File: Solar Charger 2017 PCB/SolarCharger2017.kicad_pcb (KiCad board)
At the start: 2 copper layers, 95 x 65 mm, 24 parts, among them P1 5V OUT, P2 LiIon Cell V, P3 PV IN 1, P4 PV IN 2, P5 LiIon Cell V, P6 5V OUT, P7 USB_A, SW1 5V ON, U1 BQ24210

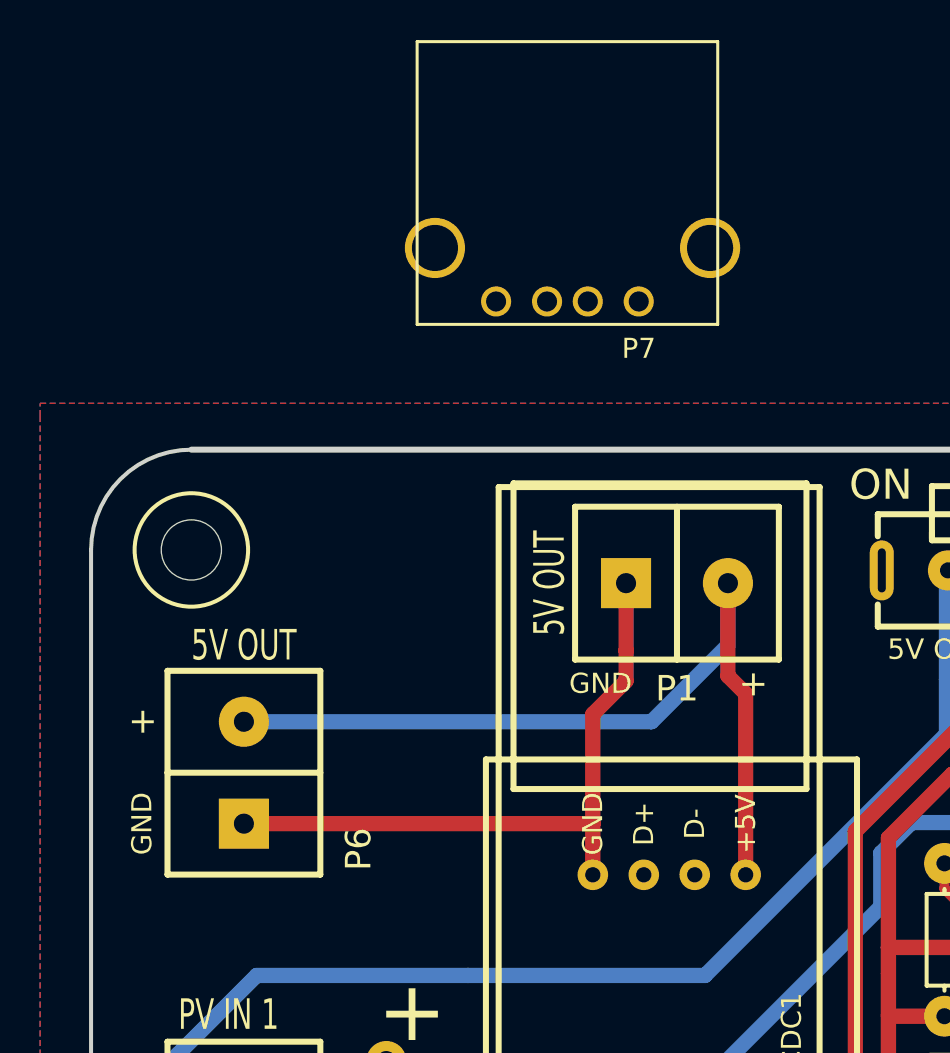
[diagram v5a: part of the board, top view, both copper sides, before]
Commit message: Update of PCB with USB output
Slight change to the USB output.
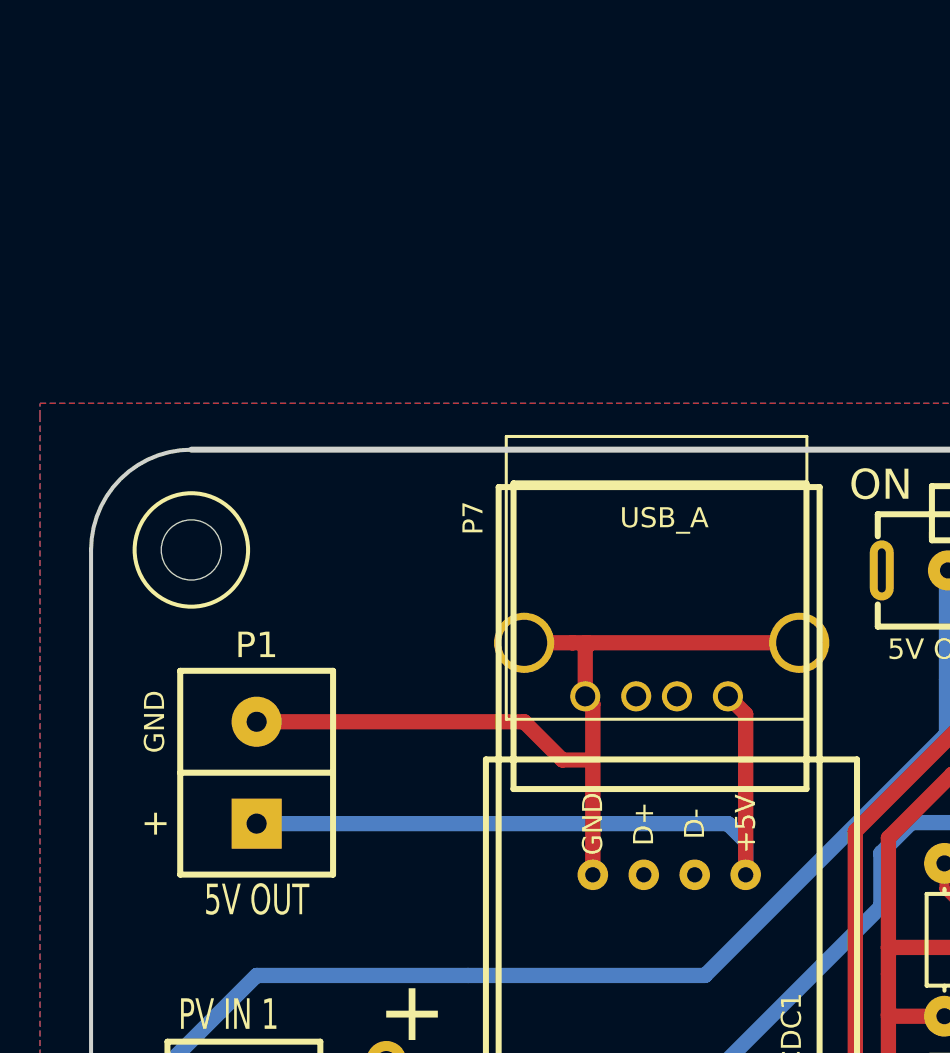
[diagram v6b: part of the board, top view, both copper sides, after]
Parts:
- removed P6: 5V OUT, REInnovationFootprint:SIL-2_screw_terminal
- moved P1 22.0 mm to (106.7, 82.5), turned to 90 degrees
- moved P7 20.2 mm to (130.2, 76.2)
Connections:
- P1 pad 1: Net-(DCDC1-Pad4) -> Net-(DCDC1-Pad3)
- P1 pad 2: Net-(DCDC1-Pad3) -> Net-(DCDC1-Pad4)
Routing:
- net Net-(DCDC1-Pad4): track 33.1 -> 43.3 mm
- net Net-(DCDC1-Pad3): track 43.7 -> 35.7 mm
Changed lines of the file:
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@@
 (kicad_pcb (version 4) (host pcbnew 4.0.5)
   (general
-    (links 51)
-    (no_connects 4)
+    (links 49)
+    (no_connects 0)
     (area 0 0 0 0)
     (thickness 1.6)
     (drawings 11)
-    (tracks 205)
+    (tracks 209)
     (zones 0)
-    (modules 24)
+    (modules 23)
     (nets 18)
   )
@@
   )
   (module REInnovationFootprint:SIL-2_screw_terminal (layer F.Cu)
-    (at 125.095 70.56)
+    (at 106.68 82.55 90)
     (descr "Connecteurs 2 pins")
     (tags "CONN DEV")
-    (fp_text reference P1 (at 2.54 5.259) (layer F.SilkS)
+    (fp_text reference P1 (at 8.89 0 180) (layer F.SilkS)
       (effects (font (thickness 0.3048)))
     )
-    (fp_text value "5V OUT" (at -3.81 0 270) (layer F.SilkS)
+    (fp_text value "5V OUT" (at -3.81 0 360) (layer F.SilkS)
       (effects (font (size 1.524 1.016) (thickness 0.254)))
     )
@@
     (fp_line (start 2.54 -3.81) (end 2.54 3.81) (layer F.SilkS) (width 0.3))
     (fp_line (start -2.54 3.81) (end -2.54 -3.81) (layer F.SilkS) (width 0.3))
-    (fp_text user GND (at -1.27 5.005) (layer F.SilkS)
+    (fp_text user GND (at 5.08 -5.08 90) (layer F.SilkS)
       (effects (font (size 1 1) (thickness 0.25)))
     )
-    (fp_text user + (at 6.35 5.005) (layer F.SilkS)
+    (fp_text user + (at 0 -5.08 90) (layer F.SilkS)
       (effects (font (thickness 0.3048)))
     )
-    (pad 1 thru_hole rect (at 0 0) (size 2.49936 2.49936) (drill 1.00076) (layers *.Cu *.Mask F.SilkS)
-      (net 12 "Net-(DCDC1-Pad4)"))
-    (pad 2 thru_hole circle (at 5.08 0) (size 2.49936 2.49936) (drill 1.00076) (layers *.Cu *.Mask F.SilkS)
+    (pad 1 thru_hole rect (at 0 0 90) (size 2.49936 2.49936) (drill 1.00076) (layers *.Cu *.Mask F.SilkS)
       (net 11 "Net-(DCDC1-Pad3)"))
+    (pad 2 thru_hole circle (at 5.08 0 90) (size 2.49936 2.49936) (drill 1.00076) (layers *.Cu *.Mask F.SilkS)
+      (net 12 "Net-(DCDC1-Pad4)"))
   )
   (module REInnovationFootprint:TH_LiIon_Holder (layer F.Cu)
@@
       (net 2 GND))
   )
-  (module REInnovationFootprint:SIL-2_screw_terminal (layer F.Cu)
-    (at 106.045 82.55 90)
-    (descr "Connecteurs 2 pins")
-    (tags "CONN DEV")
-    (fp_text reference P6 (at -1.27 5.715 270) (layer F.SilkS)
-      (effects (font (thickness 0.3048)))
-    )
-    (fp_text value "5V OUT" (at 8.89 0 180) (layer F.SilkS)
-      (effects (font (size 1.524 1.016) (thickness 0.254)))
-    )
-    (fp_line (start -2.54 3.81) (end 7.62 3.81) (layer F.SilkS) (width 0.3))
-    (fp_line (start -2.54 -3.81) (end 7.62 -3.81) (layer F.SilkS) (width 0.3))
-    (fp_line (start 7.62 3.81) (end 7.62 -3.81) (layer F.SilkS) (width 0.3))
-    (fp_line (start 2.54 -3.81) (end 2.54 3.81) (layer F.SilkS) (width 0.3))
-    (fp_line (start -2.54 3.81) (end -2.54 -3.81) (layer F.SilkS) (width 0.3))
-    (fp_text user GND (at 0 -5.08 270) (layer F.SilkS)
-      (effects (font (size 1 1) (thickness 0.25)))
-    )
-    (fp_text user + (at 5.08 -5.08 90) (layer F.SilkS)
-      (effects (font (thickness 0.3048)))
-    )
-    (pad 1 thru_hole rect (at 0 0 90) (size 2.49936 2.49936) (drill 1.00076) (layers *.Cu *.Mask F.SilkS)
-      (net 12 "Net-(DCDC1-Pad4)"))
-    (pad 2 thru_hole circle (at 5.08 0 90) (size 2.49936 2.49936) (drill 1.00076) (layers *.Cu *.Mask F.SilkS)
-      (net 11 "Net-(DCDC1-Pad3)"))
-  )
   (module REInnovationFootprint:SIL_2_screw_+_JST_2mm (layer F.Cu)
     (at 106.045 101.04 90)
@@
   )
   (module Connectors:USB_A (layer F.Cu)
-    (at 125.73 56.515 180)
+    (at 130.175 76.2 180)
     (descr "USB A connector")
     (tags "USB USB_A")
-    (fp_text reference P7 (at 0 -2.35 180) (layer F.SilkS)
+    (fp_text reference P7 (at 12.7 8.89 270) (layer F.SilkS)
       (effects (font (size 1 1) (thickness 0.15)))
     )
-    (fp_text value USB_A (at 3.83794 7.43458 180) (layer F.Fab)
+    (fp_text value USB_A (at 3.175 8.89 180) (layer F.SilkS)
       (effects (font (size 1 1) (thickness 0.15)))
     )
@@
   (segment (start 171.577 85.419) (end 171.577 83.006) (width 0.2) (layer F.Cu) (net 10))
   (segment (start 168.021 88.975) (end 171.577 85.419) (width 0.2) (layer F.Cu) (net 10))
-  (segment (start 106.045 77.47) (end 126.365 77.47) (width 0.762) (layer B.Cu) (net 11))
-  (segment (start 130.175 73.66) (end 130.175 70.56) (width 0.762) (layer B.Cu) (net 11))
-  (segment (start 126.365 77.47) (end 130.175 73.66) (width 0.762) (layer B.Cu) (net 11))
-  (segment (start 131.06 85.1) (end 131.06 76.069) (width 0.762) (layer F.Cu) (net 11))
-  (segment (start 130.175 75.184) (end 130.175 70.56) (width 0.762) (layer F.Cu) (net 11))
-  (segment (start 131.06 76.069) (end 130.175 75.184) (width 0.762) (layer F.Cu) (net 11))
-  (segment (start 106.045 82.55) (end 123.44 82.55) (width 0.762) (layer F.Cu) (net 12))
-  (segment (start 123.44 82.55) (end 123.19 82.55) (width 0.762) (layer F.Cu) (net 12))
-  (segment (start 123.19 82.55) (end 123.44 82.55) (width 0.762) (layer F.Cu) (net 12))
-  (segment (start 123.44 85.1) (end 123.44 82.55) (width 0.762) (layer F.Cu) (net 12))
-  (segment (start 123.44 82.55) (end 123.44 77.093) (width 0.762) (layer F.Cu) (net 12))
-  (segment (start 125.095 75.438) (end 125.095 73.914) (width 0.762) (layer F.Cu) (net 12))
-  (segment (start 125.095 73.914) (end 125.095 70.56) (width 0.762) (layer F.Cu) (net 12))
-  (segment (start 123.44 77.093) (end 125.095 75.438) (width 0.762) (layer F.Cu) (net 12))
+  (segment (start 106.68 82.55) (end 130.175 82.55) (width 0.762) (layer B.Cu) (net 11) (status 400000))
+  (segment (start 131.06 83.435) (end 131.06 85.1) (width 0.762) (layer B.Cu) (net 11) (status 800000))
+  (segment (start 130.175 82.55) (end 131.06 83.435) (width 0.762) (layer B.Cu) (net 11))
+  (segment (start 131.06 85.1) (end 131.06 77.08798) (width 0.762) (layer F.Cu) (net 11) (status 400000))
+  (segment (start 131.06 77.08798) (end 130.17414 76.20212) (width 0.762) (layer F.Cu) (net 11) (status 800000))
+  (segment (start 123.06214 76.20212) (end 123.06214 73.53512) (width 0.762) (layer F.Cu) (net 12) (status 400000))
+  (segment (start 123.19 73.66) (end 123.19 73.53512) (width 0.762) (layer F.Cu) (net 12))
+  (segment (start 123.18702 73.66) (end 123.19 73.66) (width 0.762) (layer F.Cu) (net 12))
+  (segment (start 123.06214 73.53512) (end 123.18702 73.66) (width 0.762) (layer F.Cu) (net 12))
+  (segment (start 122.43012 73.53512) (end 123.19 73.53512) (width 0.762) (layer F.Cu) (net 12))
+  (segment (start 123.19 73.53512) (end 133.73014 73.53512) (width 0.762) (layer F.Cu) (net 12) (status 800000))
+  (segment (start 122.43012 73.53512) (end 120.01414 73.53512) (width 0.762) (layer F.Cu) (net 12) (status 800000))
+  (segment (start 106.68 77.47) (end 120.015 77.47) (width 0.762) (layer F.Cu) (net 12) (status 400000))
+  (segment (start 121.92 79.375) (end 123.44 79.375) (width 0.762) (layer F.Cu) (net 12))
+  (segment (start 120.015 77.47) (end 121.92 79.375) (width 0.762) (layer F.Cu) (net 12))
+  (segment (start 123.44 85.1) (end 123.44 79.375) (width 0.762) (layer F.Cu) (net 12) (status 400000))
+  (segment (start 123.44 79.375) (end 123.44 76.57998) (width 0.762) (layer F.Cu) (net 12) (status 800000))
+  (segment (start 123.44 76.57998) (end 123.06214 76.20212) (width 0.762) (layer F.Cu) (net 12) (status C00000))
   (segment (start 132.945 97.97) (end 135.583 97.97) (width 0.762) (layer F.Cu) (net 13))
   (segment (start 144.15262 75.30338) (end 144.15262 69.8996) (width 0.762) (layer F.Cu) (net 13))
